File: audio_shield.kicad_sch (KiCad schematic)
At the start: 11 parts, among them J1 AudioJack2, U1 LM386, U3 OPA340NA

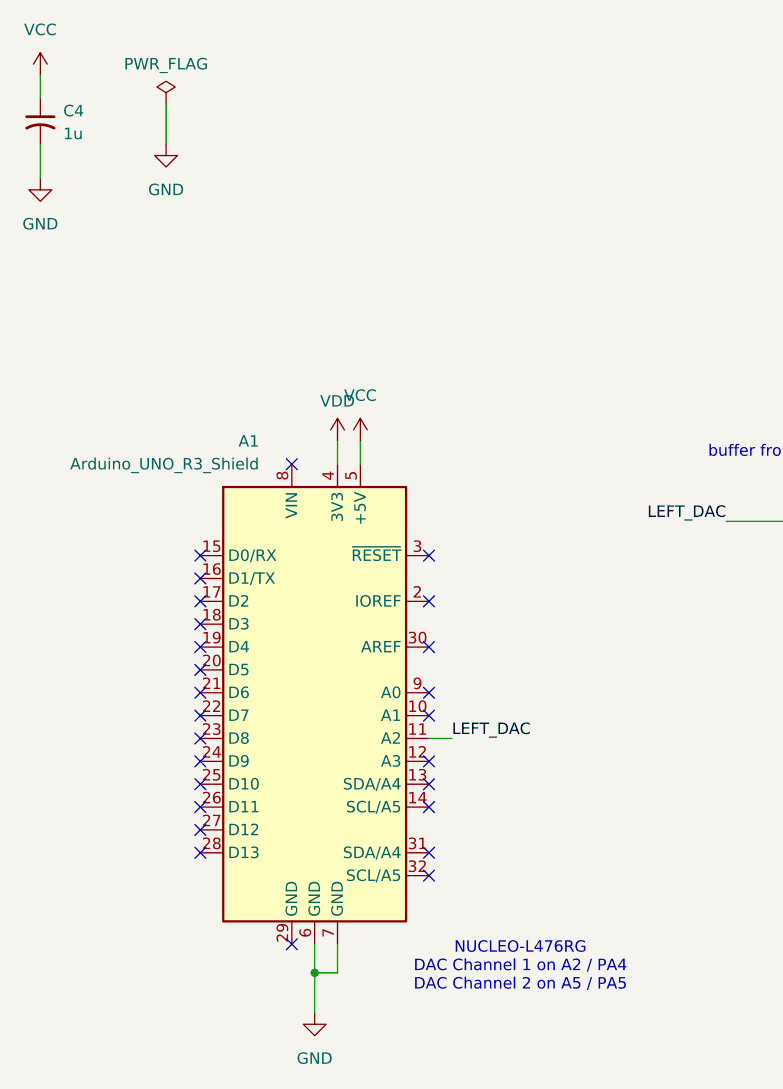
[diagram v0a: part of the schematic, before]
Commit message: fixing the project symbols and footprints path
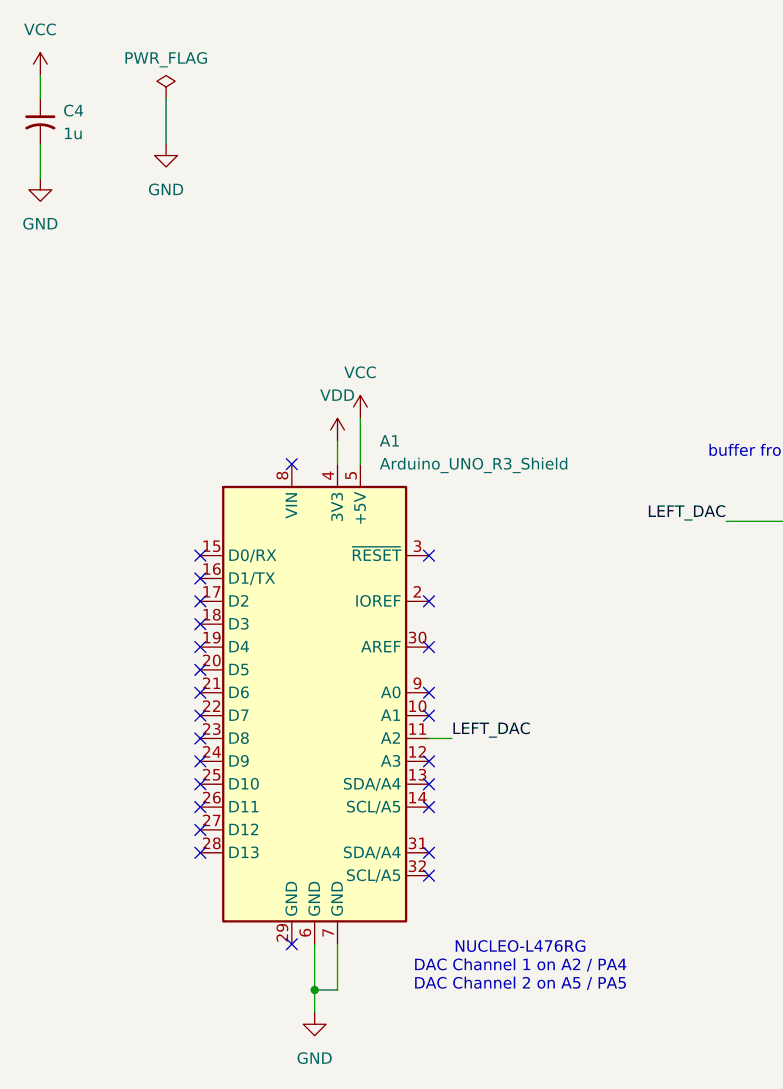
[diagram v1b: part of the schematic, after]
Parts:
- A1: symbol _MyLibrary:Arduino_UNO_R3_Shield -> _ProjectSymbols:Arduino_UNO_R3_Shield

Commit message: route the board
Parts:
- U1: footprint Package_SO:SOIC-8-1EP_3.9x4.9mm_P1.27mm_EP2.29x3mm -> Package_SO:SOIC-8_3.9x4.9mm_P1.27mm
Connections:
- net GND: now also A1.29 (GND)
- no-connect marks 29 -> 28
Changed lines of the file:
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@@
-	)
-	(no_connect
-		(at 53.34 125.73)
 	)
 	(no_connect
@@
 	(wire
 		(pts
+			(xy 213.36 86.36) (xy 214.63 86.36)
+		)
+		(stroke
+			(width 0)
+			(type default)
+		)
+	)
+	(wire
+		(pts
 			(xy 179.07 83.82) (xy 189.23 83.82)
 		)
@@
 	(wire
 		(pts
-			(xy 214.63 86.36) (xy 207.01 86.36)
-		)
-		(stroke
-			(width 0)
-			(type default)
-		)
-	)
-	(wire
-		(pts
 			(xy 128.27 81.28) (xy 129.54 81.28)
 		)
@@
 	(wire
 		(pts
+			(xy 53.34 125.73) (xy 53.34 130.81)
+		)
+		(stroke
+			(width 0)
+			(type default)
+		)
+	)
+	(wire
+		(pts
 			(xy 179.07 83.82) (xy 179.07 86.36)
 		)
@@
 	(wire
 		(pts
+			(xy 213.36 86.36) (xy 213.36 95.25)
+		)
+		(stroke
+			(width 0)
+			(type default)
+		)
+	)
+	(wire
+		(pts
 			(xy 144.78 81.28) (xy 144.78 85.09)
 		)
@@
 	(wire
 		(pts
-			(xy 207.01 86.36) (xy 207.01 93.98)
+			(xy 53.34 130.81) (xy 55.88 130.81)
 		)
 		(stroke
@@
 	(symbol
 		(lib_id "power:GND")
-		(at 207.01 93.98 0)
+		(at 213.36 95.25 0)
 		(unit 1)
 		(exclude_from_sim no)
@@
 		(fields_autoplaced yes)
 		(property "Reference" "#PWR013"
-			(at 207.01 100.33 0)
+			(at 213.36 101.6 0)
 			(effects
 				(font
@@
 		)
 		(property "Value" "GND"
-			(at 207.01 99.06 0)
+			(at 213.36 100.33 0)
 			(effects
 				(font
@@
 		)
 		(property "Footprint" ""
-			(at 207.01 93.98 0)
+			(at 213.36 95.25 0)
 			(effects
 				(font
@@
 		)
 		(property "Datasheet" ""
-			(at 207.01 93.98 0)
+			(at 213.36 95.25 0)
 			(effects
 				(font
@@
 		)
 		(property "Description" "Power symbol creates a global label with name \"GND\" , ground"
-			(at 207.01 93.98 0)
+			(at 213.36 95.25 0)
 			(effects
 				(font
@@
 			)
 		)
-		(property "Footprint" "Package_SO:SOIC-8-1EP_3.9x4.9mm_P1.27mm_EP2.29x3mm"
+		(property "Footprint" "Package_SO:SOIC-8_3.9x4.9mm_P1.27mm"
 			(at 166.37 81.28 0)
 			(effects
